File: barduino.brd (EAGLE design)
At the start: 54.9 x 47.4 mm, 28 parts, among them Q1 16MHz

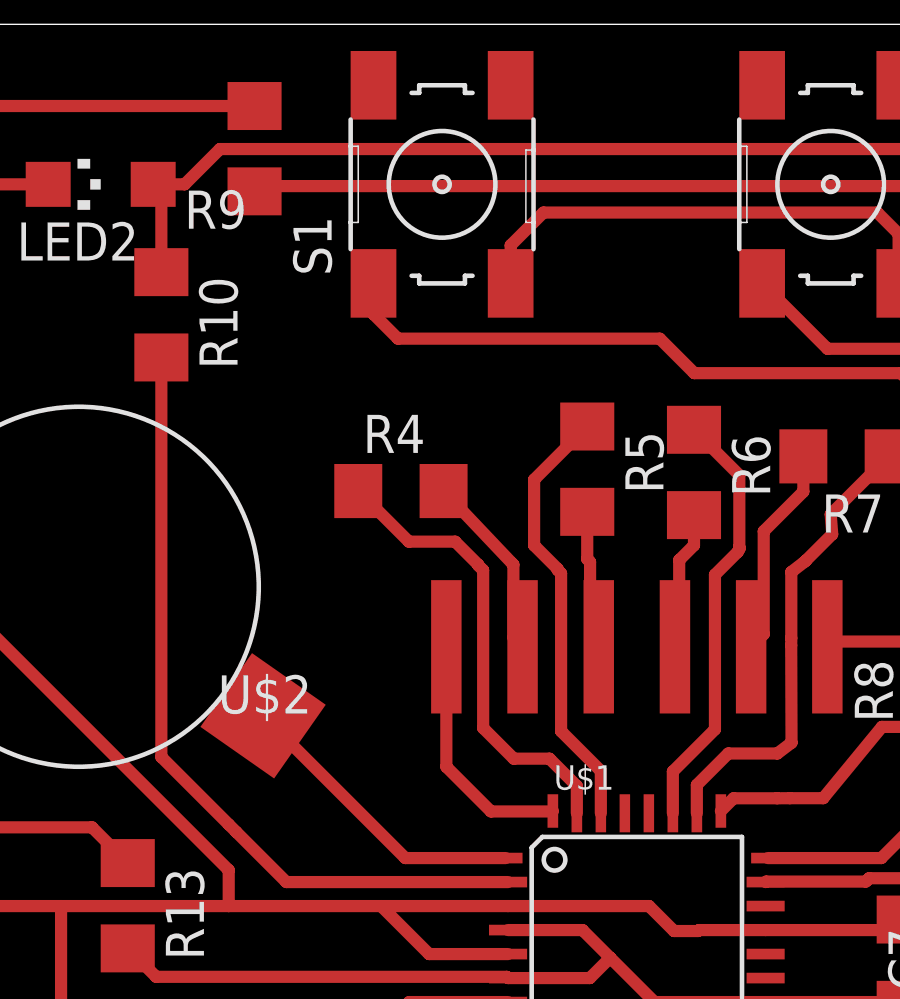
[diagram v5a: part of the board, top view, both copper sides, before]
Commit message: connected RESET
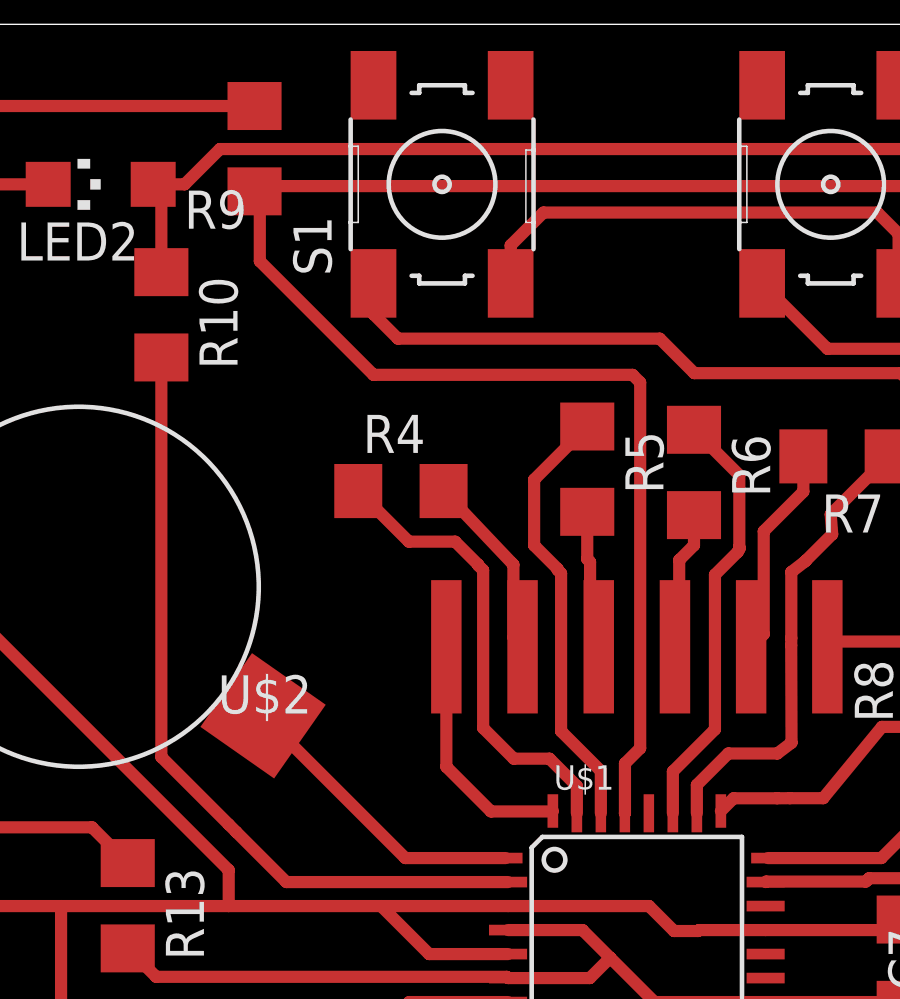
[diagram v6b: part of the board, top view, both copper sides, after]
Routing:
- net RESET: track 58.8 -> 90.2 mm
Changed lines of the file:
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@@
 <contactref element="U$1" pad="29"/>
 <contactref element="ICSP" pad="5"/>
-<wire x1="10.4103" y1="33.3909" x2="10.4255" y2="33.4061" width="0" layer="19" extent="1-16"/>
 <wire x1="31.054096875" y1="24.795546875" x2="31.8592875" y2="24.795546875" width="0.4064" layer="1"/>
 <wire x1="31.8592875" y1="24.795546875" x2="33.886440625" y2="26.8227" width="0.4064" layer="1"/>
@@
 <wire x1="33.886440625" y1="36.08548125" x2="27.947621875" y2="42.0243" width="0.4064" layer="1"/>
 <wire x1="27.947621875" y1="42.0243" x2="27.947621875" y2="46.09591875" width="0.4064" layer="1"/>
+<wire x1="10.4103" y1="33.3909" x2="10.414" y2="33.3946" width="0.4064" layer="1"/>
+<wire x1="10.414" y1="33.3946" x2="10.414" y2="35.052" width="0.4064" layer="1"/>
+<wire x1="10.414" y1="35.052" x2="10.922" y2="35.56" width="0.4064" layer="1"/>
+<wire x1="10.922" y1="47.752" x2="10.668" y2="48.006" width="0.4064" layer="1"/>
+<wire x1="10.668" y1="48.006" x2="2.032" y2="48.006" width="0.4064" layer="1"/>
+<wire x1="2.032" y1="48.006" x2="-1.7580375" y2="51.7960375" width="0.4064" layer="1"/>
+<wire x1="-1.7580375" y1="51.7960375" x2="-1.7580375" y2="54.29758125" width="0.4064" layer="1"/>
+<wire x1="10.922" y1="35.56" x2="10.922" y2="47.752" width="0.4064" layer="1"/>
 <wire x1="-1.93288125" y1="54.1227375" x2="-1.93288125" y2="54.12273125" width="0" layer="19" extent="1-1"/>
-<wire x1="10.4255" y1="33.4061" x2="27.947621875" y2="42.0243" width="0" layer="19" extent="1-1"/>
 </signal>
 <signal name="PB6">

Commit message: only a couple air wires left
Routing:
- net D3: track 10.1 -> 0.00 mm
- net GND: track 137.3 -> 138.8 mm
- net RESET: track 90.2 -> 91.4 mm
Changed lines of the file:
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@@
 <setting verticaltext="up"/>
 </settings>
-<grid distance="0.01" unitdist="inch" unit="inch" style="lines" multiple="1" display="no" altdistance="0.025" altunitdist="inch" altunit="inch"/>
+<grid distance="0.0001" unitdist="inch" unit="inch" style="lines" multiple="1" display="no" altdistance="0.025" altunitdist="inch" altunit="inch"/>
 <layers>
 <layer number="1" name="Top" color="12" fill="1" visible="yes" active="yes"/>
@@
 <wire x1="26.518" y1="40.97741875" x2="32.8168" y2="34.67861875" width="0.4064" layer="1"/>
 <contactref element="R13" pad="1"/>
-<wire x1="6.5177" y1="27.8983" x2="6.476" y2="27.94" width="0.4064" layer="1"/>
 <contactref element="U$5" pad="VBUS"/>
 <contactref element="R13" pad="2"/>
-<wire x1="-5.21168125" y1="27.94" x2="-6.1595" y2="28.88781875" width="0.4064" layer="1"/>
-<wire x1="6.476" y1="27.94" x2="-5.21168125" y2="27.94" width="0.4064" layer="1"/>
 <wire x1="-15.687" y1="32.923" x2="-11.079" y2="32.923" width="0.4064" layer="1"/>
 <wire x1="-11.079" y1="32.923" x2="-7.35068125" y2="32.923" width="0.4064" layer="1"/>
@@
 <wire x1="-7.35068125" y1="32.923" x2="-6.1595" y2="31.73181875" width="0.4064" layer="1"/>
 <wire x1="-17.455271875" y1="56.966728125" x2="-1.932884375" y2="56.966728125" width="0.4064" layer="1"/>
-<wire x1="-1.932884375" y1="56.966728125" x2="-1.93288125" y2="56.96673125" width="0" layer="19" extent="1-1"/>
-<wire x1="-6.1595" y1="28.88781875" x2="-6.1595" y2="31.73181875" width="0" layer="19" extent="1-1"/>
+<wire x1="-1.932884375" y1="56.966728125" x2="-1.93288125" y2="56.96673125" width="0.635" layer="1"/>
+<wire x1="-1.82245" y1="57.01665" x2="-1.932884375" y2="56.966728125" width="0.635" layer="1"/>
+<wire x1="6.5177" y1="27.8983" x2="-5.16998125" y2="27.8983" width="0.4064" layer="1"/>
+<wire x1="-5.16998125" y1="27.8983" x2="-6.1595" y2="28.88781875" width="0.4064" layer="1"/>
+<wire x1="-6.1595" y1="31.73181875" x2="-6.1595" y2="28.88781875" width="0" layer="19" extent="1-1"/>
 </signal>
 <signal name="GND" class="1">
@@
 <wire x1="-12.628825" y1="21.47535625" x2="-12.882825" y2="21.47535625" width="0.4064" layer="1"/>
 <wire x1="-8.382" y1="30.2983" x2="-14.32519375" y2="30.2983" width="0.4064" layer="1"/>
-<wire x1="-14.32519375" y1="30.2983" x2="-14.35949375" y2="30.3326" width="0.4064" layer="1"/>
 <wire x1="-14.35949375" y1="30.3326" x2="-15.687" y2="30.3326" width="0.4064" layer="1"/>
 <wire x1="-2.794" y1="30.2983" x2="-2.794" y2="31.496" width="0.4064" layer="1"/>
 <wire x1="-15.71435625" y1="54.216525" x2="-15.57488125" y2="54.356" width="0.4064" layer="1"/>
-<wire x1="-2.794" y1="31.496" x2="-13.93635625" y2="42.63835625" width="0.4064" layer="1"/>
-<wire x1="-13.93635625" y1="42.63835625" x2="-13.93635625" y2="45.24408125" width="0.4064" layer="1"/>
+<wire x1="6.5177" y1="28.6983" x2="3.886" y2="28.6983" width="0.4064" layer="1"/>
+<wire x1="3.886" y1="28.6983" x2="2.286" y2="30.2983" width="0.4064" layer="1"/>
 <wire x1="-15.57488125" y1="54.356" x2="-15.57488125" y2="46.88260625" width="0.4064" layer="1"/>
 <wire x1="-15.57488125" y1="46.88260625" x2="-13.93635625" y2="45.24408125" width="0.4064" layer="1"/>
-<wire x1="6.5177" y1="28.6983" x2="3.886" y2="28.6983" width="0.4064" layer="1"/>
-<wire x1="3.886" y1="28.6983" x2="2.286" y2="30.2983" width="0.4064" layer="1"/>
-<wire x1="-13.93635625" y1="45.24408125" x2="-13.93635625" y2="45.244084375" width="0" layer="19" extent="1-1"/>
-<wire x1="-15.687" y1="30.323" x2="-15.687" y2="30.3326" width="0" layer="19" extent="1-1"/>
+<wire x1="-13.93635625" y1="42.63835625" x2="-2.794" y2="31.496" width="0.4064" layer="1"/>
+<wire x1="-13.93635625" y1="45.24408125" x2="-13.93635625" y2="42.63835625" width="0.4064" layer="1"/>
+<wire x1="-15.687" y1="30.323" x2="-14.36909375" y2="30.323" width="0.4064" layer="1"/>
+<wire x1="-14.36909375" y1="30.323" x2="-14.35949375" y2="30.3326" width="0.4064" layer="1"/>
+<wire x1="-14.32519375" y1="30.2983" x2="-14.35949375" y2="30.3326" width="0.4064" layer="1"/>
+<wire x1="-13.93635625" y1="45.24408125" x2="-13.93635625" y2="45.244084375" width="0.635" layer="1"/>
+<wire x1="-13.79855" y1="45.3009" x2="-13.93635625" y2="45.24408125" width="0.635" layer="1"/>
 </signal>
 <signal name="PB7">
@@
 <wire x1="21.07691875" y1="53.0606" x2="21.50871875" y2="52.59578125" width="0.4064" layer="1"/>
 <wire x1="27.947621875" y1="46.09591875" x2="21.50871875" y2="52.59578125" width="0.4064" layer="1"/>
-<wire x1="19.8399375" y1="54.29758125" x2="-1.7580375" y2="54.29758125" width="0.4064" layer="1"/>
-<wire x1="-1.7580375" y1="54.29758125" x2="-1.93288125" y2="54.1227375" width="0.4064" layer="1"/>
+<wire x1="19.8399375" y1="54.29758125" x2="-1.016" y2="54.29758125" width="0.4064" layer="1"/>
+<wire x1="-1.016" y1="54.29758125" x2="-1.7580375" y2="54.29758125" width="0.4064" layer="1"/>
 <wire x1="33.886440625" y1="36.08548125" x2="27.947621875" y2="42.0243" width="0.4064" layer="1"/>
 <wire x1="27.947621875" y1="42.0243" x2="27.947621875" y2="46.09591875" width="0.4064" layer="1"/>
@@
 <wire x1="10.668" y1="48.006" x2="2.032" y2="48.006" width="0.4064" layer="1"/>
 <wire x1="2.032" y1="48.006" x2="-1.7580375" y2="51.7960375" width="0.4064" layer="1"/>
-<wire x1="-1.7580375" y1="51.7960375" x2="-1.7580375" y2="54.29758125" width="0.4064" layer="1"/>
+<wire x1="-1.7580375" y1="51.7960375" x2="-1.7580375" y2="54.1528" width="0.4064" layer="1"/>
+<wire x1="-1.7580375" y1="54.1528" x2="-1.7580375" y2="54.29758125" width="0.4064" layer="1"/>
 <wire x1="10.922" y1="35.56" x2="10.922" y2="47.752" width="0.4064" layer="1"/>
-<wire x1="-1.93288125" y1="54.1227375" x2="-1.93288125" y2="54.12273125" width="0" layer="19" extent="1-1"/>
+<wire x1="-1.93288125" y1="54.1227375" x2="-1.7580375" y2="54.29758125" width="0.4064" layer="1"/>
+<wire x1="-1.93288125" y1="54.1227375" x2="-1.19084375" y2="54.1227375" width="0.4064" layer="1"/>
+<wire x1="-1.19084375" y1="54.1227375" x2="-1.016" y2="54.29758125" width="0.4064" layer="1"/>
+<wire x1="-1.82245" y1="54.1528" x2="-1.93288125" y2="54.12273125" width="0.635" layer="1"/>
+<wire x1="-1.82245" y1="54.1528" x2="-1.7580375" y2="54.1528" width="0.635" layer="1"/>
 </signal>
 <signal name="PB6">
@@
 <contactref element="U$1" pad="1"/>
 <contactref element="U$4" pad="P$1"/>
-<wire x1="6.4415" y1="31.8983" x2="3.09305625" y2="31.8983" width="0.4064" layer="1"/>
-<wire x1="3.09305625" y1="31.8983" x2="-1.649078125" y2="36.640434375" width="0.4064" layer="1"/>
-<wire x1="-1.649078125" y1="36.640434375" x2="-1.649078125" y2="36.6404375" width="0" layer="19" extent="1-1"/>
+<wire x1="-1.649078125" y1="36.6404375" x2="6.4415" y2="31.8983" width="0" layer="19" extent="1-1"/>
 </signal>
 <signal name="D4">
@@
 <contactref element="R10" pad="2"/>
 <wire x1="6.5177" y1="31.0983" x2="-0.8723" y2="31.0983" width="0.4064" layer="1"/>
-<wire x1="-0.8723" y1="31.0983" x2="-2.54" y2="32.766" width="0.4064" layer="1"/>
-<wire x1="-2.54" y1="32.766" x2="-2.794" y2="33.02" width="0.4064" layer="1"/>
-<wire x1="-2.794" y1="33.02" x2="-5.0393625" y2="35.2653625" width="0.4064" layer="1"/>
+<wire x1="-0.8723" y1="31.0983" x2="-5.0393625" y2="35.2653625" width="0.4064" layer="1"/>
 <wire x1="-5.0393625" y1="35.2653625" x2="-5.0393625" y2="48.585521875" width="0.4064" layer="1"/>
 </signal>

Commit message: finally fixed that buzzer connection
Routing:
- net D3: track 0.00 -> 9.97 mm
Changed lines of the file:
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@@
 <autorouter>
 <pass name="Default">
-<param name="RoutingGrid" value="50mil"/>
+<param name="RoutingGrid" value="12.5mil"/>
 <param name="AutoGrid" value="1"/>
 <param name="Efforts" value="0"/>
@@
 <param name="PrefDir.14" value="0"/>
 <param name="PrefDir.15" value="0"/>
-<param name="PrefDir.16" value="-"/>
+<param name="PrefDir.16" value="0"/>
 <param name="cfVia" value="8"/>
 <param name="cfNonPref" value="5"/>
@@
 <contactref element="U$1" pad="1"/>
 <contactref element="U$4" pad="P$1"/>
-<wire x1="-1.649078125" y1="36.6404375" x2="6.4415" y2="31.8983" width="0" layer="19" extent="1-1"/>
+<wire x1="-0.04318125" y1="35.466021875" x2="-1.5875" y2="36.5125" width="0.4064" layer="1"/>
+<wire x1="6.4415" y1="31.8983" x2="5.379721875" y2="31.89478125" width="0.4064" layer="1"/>
+<wire x1="-1.5875" y1="36.5125" x2="-1.649078125" y2="36.6404375" width="0.635" layer="1"/>
+<wire x1="5.379721875" y1="31.89478125" x2="3.528059375" y2="31.89478125" width="0.4064" layer="1"/>
+<wire x1="3.528059375" y1="31.89478125" x2="-0.04318125" y2="35.466021875" width="0.4064" layer="1"/>
 </signal>
 <signal name="D4">
